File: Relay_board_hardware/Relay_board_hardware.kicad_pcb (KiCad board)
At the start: 2 copper layers, 101.6 x 127 mm, 23 parts, among them IC1 BTS3800SL, Q1 Q_NMOS_GDS, U1 Opamp_Dual

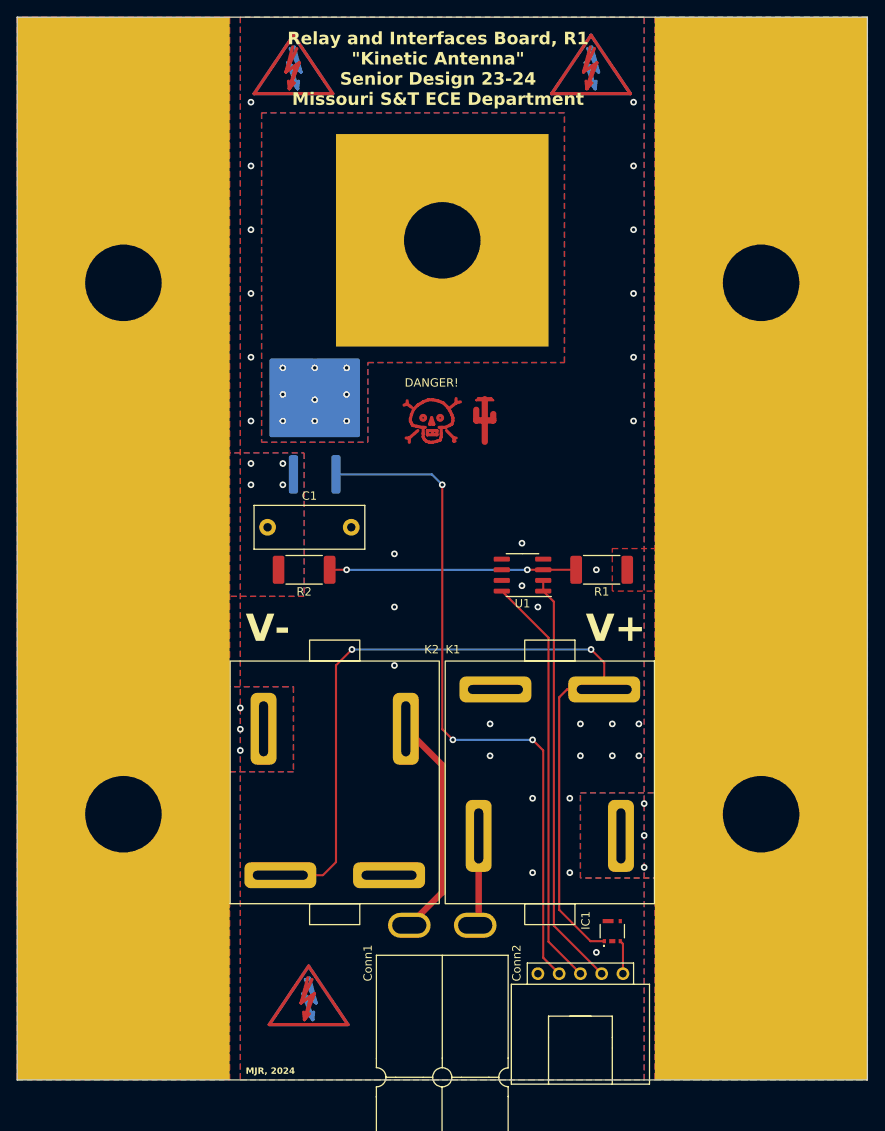
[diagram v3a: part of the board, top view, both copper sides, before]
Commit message: board review changes made
major revisions: curved corners, relocated DSCHG resistor pad, cosmetics. Final dimensions 4x4"
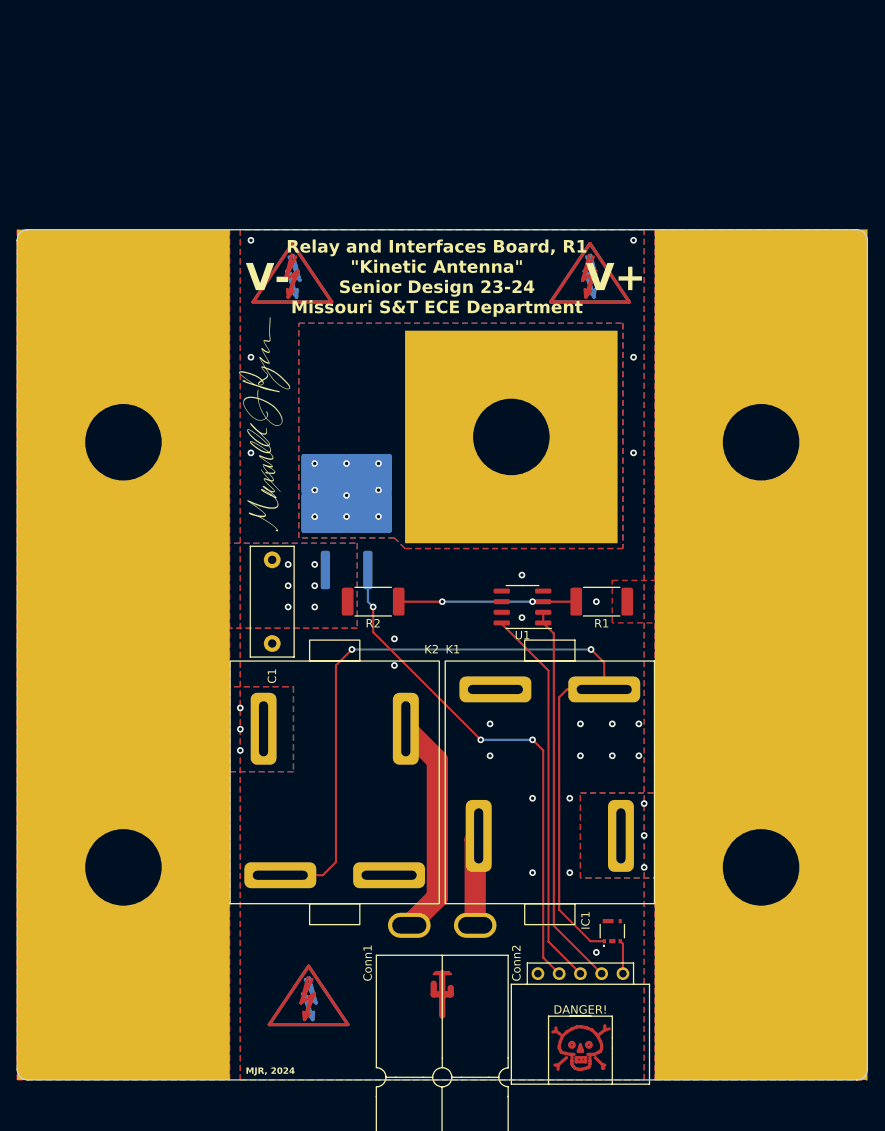
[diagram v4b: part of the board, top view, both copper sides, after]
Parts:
- added G***: LOGO, MRDT_Silkscreens:z_sig_MaxRyan_25x6.6mm, F.Cu at (131.1, 74.2)
- added G***: LOGO, MRDT_Silkscreens:yagi, B.Cu at (152.4, 55.9)
- C1: value 4.7u -> 4.7n
- V2, V3, V4, V5: footprint 0-customs:via_L2500mil_W1000mil -> 0-customs:via_L2000mil_W1000mil
- moved DANGER! 77.0 mm to (168.9, 148.6)
- moved REF** 68.8 mm to (152.4, 134.6)
- moved V1 24.9 mm to (160.7, 75.6)
- moved REF** 24.9 mm to (170.1, 56.6) (x2)
- moved REF** 24.9 mm to (134.5, 56.6) (x2)
- moved V2 19.1 mm to (190.5, 76.2)
- moved V3 19.1 mm to (114.3, 76.2)
- moved Q1 12.0 mm to (141.0, 83.8)
- moved R2 9.09 mm to (144.1, 95.2)
- moved V4 6.35 mm to (190.5, 127.0)
- moved V5 6.35 mm to (114.3, 127.0)
- moved C1 3.93 mm to (132.1, 90.2), turned to -90 degrees
- moved R1 3.81 mm to (171.4, 95.2)
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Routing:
- net DSCHG_IN: track 83.0 -> 61.3 mm
- net Net-(U1A-+): track 29.5 -> 21.2 mm
- net /V_SENSE_OUT: track 49.9 -> 46.1 mm
- net +3V3: track 49.6 -> 45.8 mm
- net GNDPWR: vias 7 -> 9
- net GND: vias 32 -> 24
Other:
- board size 101.6 x 127 mm -> 101.6 x 101.6 mm
